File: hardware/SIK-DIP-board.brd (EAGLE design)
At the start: 91.4 x 66 mm, 72 parts

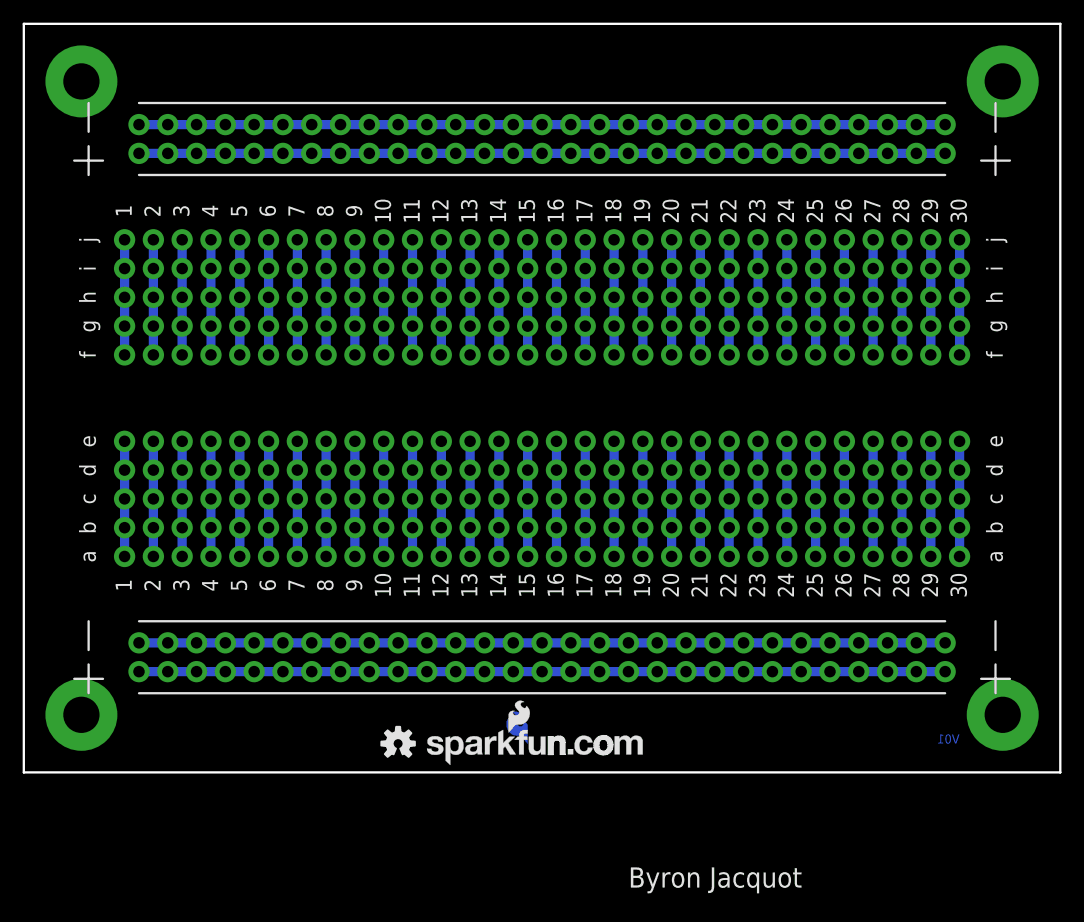
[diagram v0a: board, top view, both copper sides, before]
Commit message: Added pads to allow grounding via mounting holes.
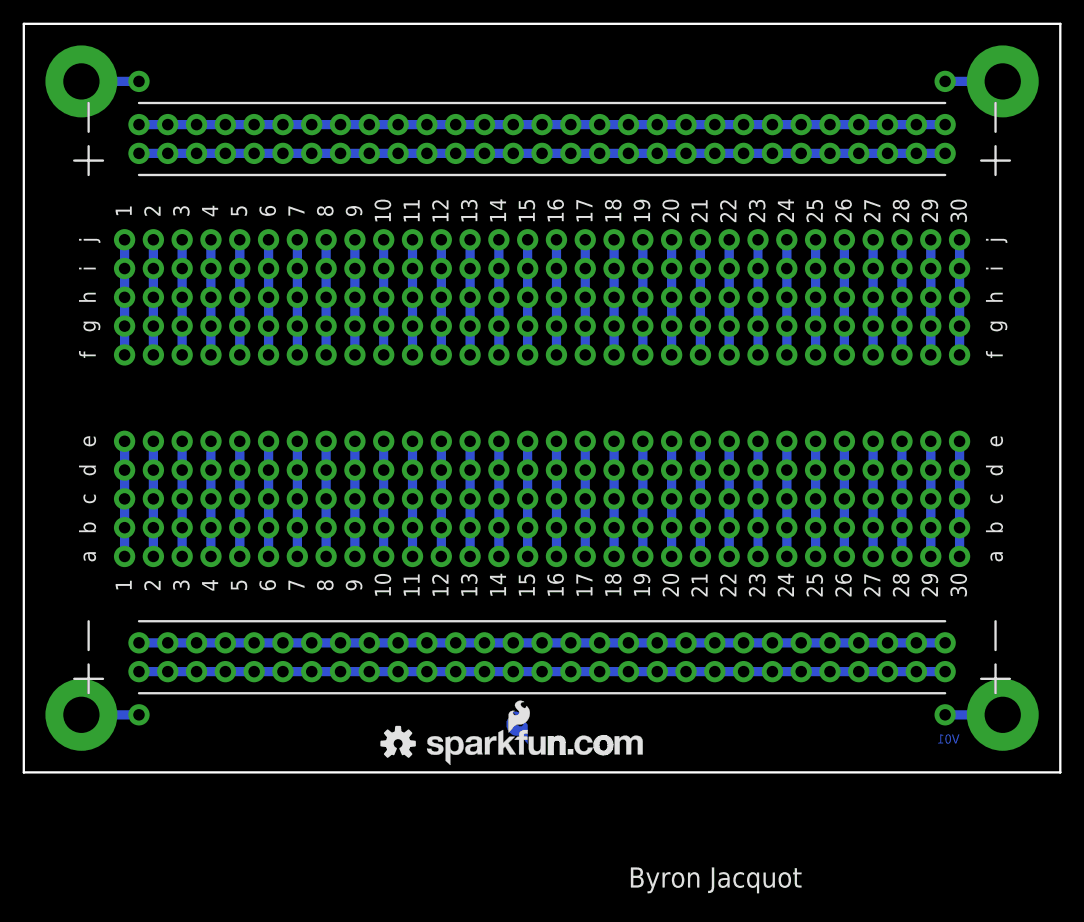
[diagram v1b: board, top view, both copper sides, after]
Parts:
- added JP65, JP66, JP67, JP68: M01SMDNS, SparkFun-Connectors:1X01NS
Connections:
- new net N$65: JP65.1, S2.P1
- new net N$66: JP66.1, S1.P1
- new net N$67: JP67.1, S3.P1
- new net N$68: JP68.1, S4.P1
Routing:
- net N$67: track 0.00 -> 5.08 mm
- net N$66: track 0.00 -> 5.08 mm
- net N$68: track 0.00 -> 5.08 mm
- net N$65: track 0.00 -> 5.08 mm
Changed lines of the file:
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@@
 <element name="JP4" library="SparkFun-Connectors" package="1X29_NO_SILK" value="M29NO_SILK" x="10.16" y="8.89" smashed="yes"/>
 <element name="LOGO3" library="SparkFun-Aesthetics" package="OSHW-LOGO-S" value="OSHW-LOGOS" x="33.02" y="2.54"/>
+<element name="JP65" library="SparkFun-Connectors" package="1X01NS" value="M01SMDNS" x="81.28" y="60.96"/>
+<element name="JP66" library="SparkFun-Connectors" package="1X01NS" value="M01SMDNS" x="10.16" y="60.96"/>
+<element name="JP67" library="SparkFun-Connectors" package="1X01NS" value="M01SMDNS" x="10.16" y="5.08"/>
+<element name="JP68" library="SparkFun-Connectors" package="1X01NS" value="M01SMDNS" x="81.28" y="5.08"/>
 </elements>
 <signals>
@@
 <wire x1="78.74" y1="8.89" x2="81.28" y2="8.89" width="0.8128" layer="16"/>
 </signal>
+<signal name="N$65">
+<contactref element="S2" pad="P1"/>
+<contactref element="JP65" pad="1"/>
+<wire x1="81.28" y1="60.96" x2="86.36" y2="60.96" width="0.8128" layer="16"/>
+</signal>
+<signal name="N$66">
+<contactref element="S1" pad="P1"/>
+<contactref element="JP66" pad="1"/>
+<wire x1="10.16" y1="60.96" x2="5.08" y2="60.96" width="0.8128" layer="16"/>
+</signal>
+<signal name="N$67">
+<contactref element="S3" pad="P1"/>
+<contactref element="JP67" pad="1"/>
+<wire x1="10.16" y1="5.08" x2="5.08" y2="5.08" width="0.8128" layer="16"/>
+</signal>
+<signal name="N$68">
+<contactref element="S4" pad="P1"/>
+<contactref element="JP68" pad="1"/>
+<wire x1="81.28" y1="5.08" x2="86.36" y2="5.08" width="0.8128" layer="16"/>
+</signal>
 </signals>
